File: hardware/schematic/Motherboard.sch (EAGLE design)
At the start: 111 parts, among them J1 POWER_JACKPTH, Q1 8MHz, Q2 32.768KHz, T1 LF-TRIACSOT223, T10 LF-TRIACSOT223, T11 LF-TRIACSOT223, T12 LF-TRIACSOT223, T13 LF-TRIACSOT223, T14 LF-TRIACSOT223, T15 LF-TRIACSOT223, T16 LF-TRIACSOT223, T2 LF-TRIACSOT223, T3 LF-TRIACSOT223, T4 LF-TRIACSOT223, T5 LF-TRIACSOT223, T6 LF-TRIACSOT223, T7 LF-TRIACSOT223, T8 LF-TRIACSOT223, T9 LF-TRIACSOT223, U1 PIC32MX460F512L TQFP100, U2 RECOM_X.X_REG78XX

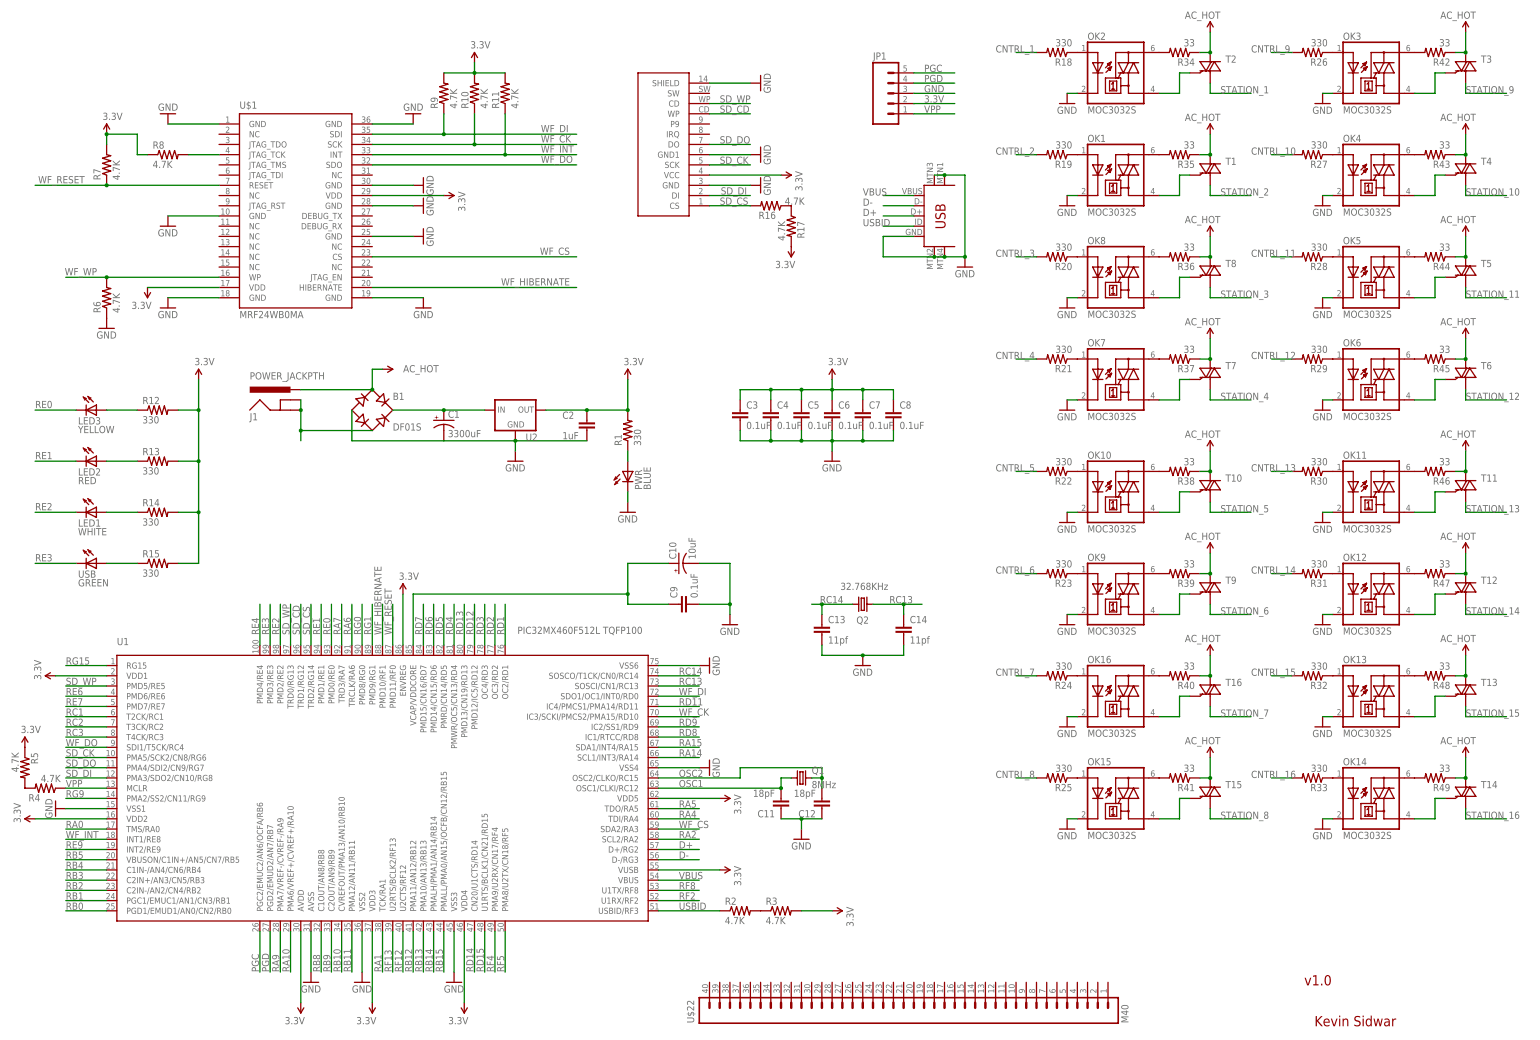
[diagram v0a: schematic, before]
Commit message: Increase trace widths on Power board.  Start motherboard layout
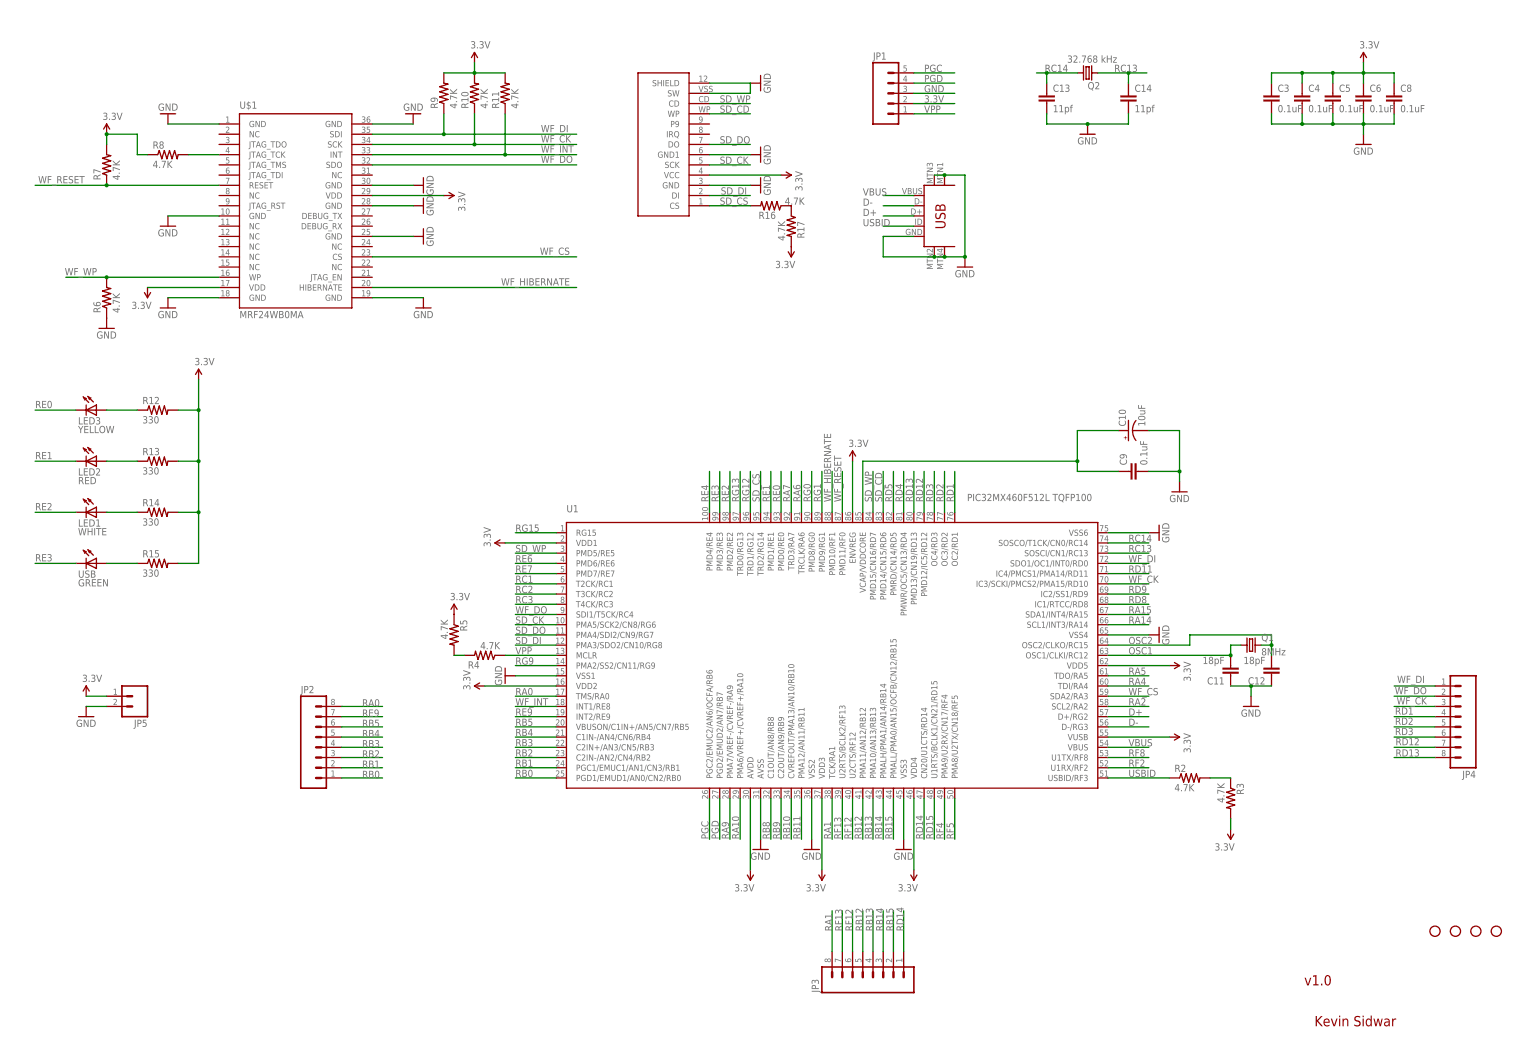
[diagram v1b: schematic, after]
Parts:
- removed B1: DF01S, lizardworx:DF01S
- removed C1: 3300uF, rcl:CPOL-USE10-20
- removed C2: 1uF, SparkFun-Passives:CAP0402-CAP
- removed C7: 0.1uF, SparkFun02-20-08:CAP0402
- removed J1: POWER_JACKPTH, lizardworx:POWER_JACKPTH
- removed OK1, OK10, OK11, OK12, OK13, OK14, OK15, OK16, OK2, OK3, OK4, OK5, OK6, OK7, OK8, OK9: MOC3032S, lizardworx:MOC3032S
- removed PWR: BLUE, SparkFun:LED0603
- removed R1, R18, R19, R20, R21, R22, R23, R24, R25, R26, R27, R28, R29, R30, R31, R32, R33: 330, SparkFun-Passives:RESISTOR0603-RES
- removed R34, R35, R36, R37, R38, R39, R40, R41, R42, R43, R44, R45, R46, R47, R48, R49: 33, SparkFun-Passives:RESISTOR0603-RES
- removed T1, T10, T11, T12, T13, T14, T15, T16, T2, T3, T4, T5, T6, T7, T8, T9: LF-TRIACSOT223, lizardworx:LF-TRIACSOT223
- removed U$22: M40, SparkFun-Connectors:M40
- removed U$3: SD_CARD_SOCKETSD, SparkFun-Connectors:SD_CARD_SOCKETSD
- removed U2: RECOM_X.X_REG78XX, lizardworx:RECOM_X.X_REG78XX
- added JP2, JP3, JP4: (no value), SparkFun-Connectors:M08LOCK
- added JP5: (no value), SparkFun-Connectors:M02LOCK
- added JP6, JP7, JP8, JP9: STAND-OFF, lizardworx:STAND-OFF
- added U$2: SD_CARD_SOCKETALPS, lizardworx:SD_CARD_SOCKETALPS
- C11, C12, C13, C14, C3, C4, C5, C6, C8, C9: device SparkFun:CAP0402 -> SparkFun:CAP0603
- Q2: value 32.768KHz -> 32.768 kHz; device SchmalzHaus:CRYSTAL32-SMD -> lizardworx:CRYSTAL
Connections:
- removed net AC_HOT: B1.AC1, J1.PWR, R34.1, R35.1, R36.1, R37.1, R38.1, R39.1, R40.1, R41.1, R42.1, R43.1, R44.1, R45.1, R46.1, R47.1, R48.1, R49.1, T1.A2, T10.A2, T11.A2, T12.A2, T13.A2, T14.A2, T15.A2, T16.A2, T2.A2, T3.A2, T4.A2, T5.A2, T6.A2, T7.A2, T8.A2, T9.A2
- removed net AC_NEUTRAL: B1.AC2, J1.GND, J1.GNDBREAK
- removed net CNTRL_1: R18.2
- removed net CNTRL_10: R27.2
- removed net CNTRL_11: R28.2
- removed net CNTRL_12: R29.2
- removed net CNTRL_13: R30.2
- removed net CNTRL_14: R31.2
- removed net CNTRL_15: R32.2
- removed net CNTRL_16: R33.2
- removed net CNTRL_2: R19.2
- removed net CNTRL_3: R20.2
- removed net CNTRL_4: R21.2
- removed net CNTRL_5: R22.2
- removed net CNTRL_6: R23.2
- removed net CNTRL_7: R24.2
- removed net CNTRL_8: R25.2
- removed net CNTRL_9: R26.2
- removed net N$1: OK9.A, R23.1
- removed net N$12: OK2.A2, R34.2
- removed net N$13: OK9.A1, T9.G
- removed net N$14: OK2.A1, T2.G
- removed net N$17: OK3.A, R26.1
- removed net N$18: OK3.A2, R42.2
- removed net N$2: OK1.A, R19.1
- removed net N$21: OK3.A1, T3.G
- removed net N$26: OK4.A, R27.1
- removed net N$27: OK4.A2, R43.2
- removed net N$28: OK10.A, R22.1
- removed net N$29: OK4.A1, T4.G
- removed net N$3: B1.+, C1.+, U2.IN
- removed net N$32: OK5.A, R28.1
- removed net N$33: OK5.A2, R44.2
- removed net N$34: OK10.A2, R38.2
- removed net N$36: OK5.A1, T5.G
- removed net N$39: OK6.A, R29.1
- removed net N$4: PWR.A, R1.1
- removed net N$40: OK6.A2, R45.2
- removed net N$41: OK10.A1, T10.G
- removed net N$42: OK6.A1, T6.G
- removed net N$45: OK7.A, R21.1
- removed net N$46: OK7.A2, R37.2
- removed net N$48: OK7.A1, T7.G
- removed net N$51: OK8.A, R20.1
- removed net N$52: OK8.A2, R36.2
- removed net N$53: OK11.A, R30.1
- removed net N$54: OK8.A1, T8.G
- removed net N$57: OK11.A2, R46.2
- removed net N$58: OK11.A1, T11.G
- removed net N$6: OK1.A2, R35.2
- removed net N$61: OK12.A, R31.1
- removed net N$62: OK12.A2, R47.2
- removed net N$63: OK12.A1, T12.G
- removed net N$66: OK13.A, R32.1
- removed net N$67: OK13.A2, R48.2
- removed net N$68: OK13.A1, T13.G
- removed net N$7: OK9.A2, R39.2
- removed net N$71: OK14.A, R33.1
- removed net N$72: OK14.A2, R49.2
- removed net N$73: OK14.A1, T14.G
- removed net N$76: OK15.A, R25.1
- removed net N$77: OK15.A2, R41.2
- removed net N$78: OK15.A1, T15.G
- removed net N$8: OK1.A1, T1.G
- removed net N$81: OK16.A, R24.1
- removed net N$82: OK16.A2, R40.2
- removed net N$83: OK16.A1, T16.G
- removed net N$9: OK2.A, R18.1
- removed net RD6: U1.PMD14/CN15/RD6
- removed net RD7: U1.PMD15/CN16/RD7
- removed net STATION_1: T2.A1
- removed net STATION_10: T4.A1
- removed net STATION_11: T5.A1
- removed net STATION_12: T6.A1
- removed net STATION_13: T11.A1
- removed net STATION_14: T12.A1
- removed net STATION_15: T13.A1
- removed net STATION_16: T14.A1
- removed net STATION_2: T1.A1
- removed net STATION_3: T8.A1
- removed net STATION_4: T7.A1
- removed net STATION_5: T10.A1
- removed net STATION_6: T9.A1
- removed net STATION_7: T16.A1
- removed net STATION_8: T15.A1
- removed net STATION_9: T3.A1
- new net RG12: U1.TRD1/RG12
- new net RG13: U1.TRD0/RG13
- net 3.3V: now also JP5.1, U$2.VCC; no longer C2.1, C7.1, R1.2, U$3.VCC, U2.OUT
- net GND: now also JP5.2, U$2.GND, U$2.GND1, U$2.SHIELD, U$2.SW; no longer B1.-, C1.-, C2.2, C7.2, OK1.C, OK10.C, OK11.C, OK12.C, OK13.C, OK14.C, OK15.C, OK16.C, OK2.C, OK3.C, OK4.C, OK5.C, OK6.C, OK7.C, OK8.C, OK9.C, PWR.C, U$3.GND, U$3.GND1, U$3.SHIELD, U2.GND
- net RA0: now also JP2.8
- net RA1: now also JP3.8
- net RB0: now also JP2.1
- net RB1: now also JP2.2
- net RB12: now also JP3.5
- net RB13: now also JP3.4
- net RB14: now also JP3.3
- net RB15: now also JP3.2
- net RB2: now also JP2.3
- net RB3: now also JP2.4
- net RB4: now also JP2.5
- net RB5: now also JP2.6
- net RC13: now also Q2.2; no longer Q2.1
- net RC14: now also Q2.1; no longer Q2.2
- net RD1: now also JP4.4
- net RD12: now also JP4.7
- net RD13: now also JP4.8
- net RD14: now also JP3.1
- net RD2: now also JP4.5
- net RD3: now also JP4.6
- net RE9: now also JP2.7
- net RF12: now also JP3.6
- net RF13: now also JP3.7
- net SD_CD: now also U$2.WP, U1.PMD14/CN15/RD6; no longer U$3.WP, U1.TRD1/RG12
- net SD_CK: now also U$2.SCK; no longer U$3.SCK
- net SD_CS: now also U$2.CS; no longer U$3.CS
- net SD_DI: now also U$2.DI; no longer U$3.DI
- net SD_DO: now also U$2.DO; no longer U$3.DO
- net SD_WP: now also U$2.CD, U1.PMD15/CN16/RD7; no longer U$3.CD, U1.TRD0/RG13
- net WF_CK: now also JP4.3
- net WF_DI: now also JP4.1
- net WF_DO: now also JP4.2
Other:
- moved on the sheet: C10, C11, C12, C13, C14, C3, C4, C5, C6, C8, C9, Q1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
